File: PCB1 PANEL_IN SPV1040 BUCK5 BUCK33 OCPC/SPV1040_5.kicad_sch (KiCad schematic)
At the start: 14 parts, among them J6 SOLAR, U6 SPV1040TTR

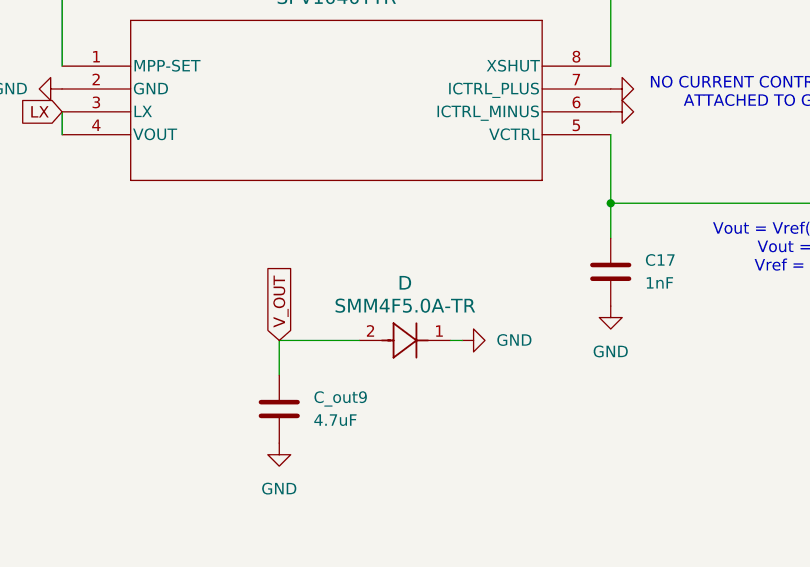
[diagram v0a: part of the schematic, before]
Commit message: Added some comments in POWERPCB, about bus interface
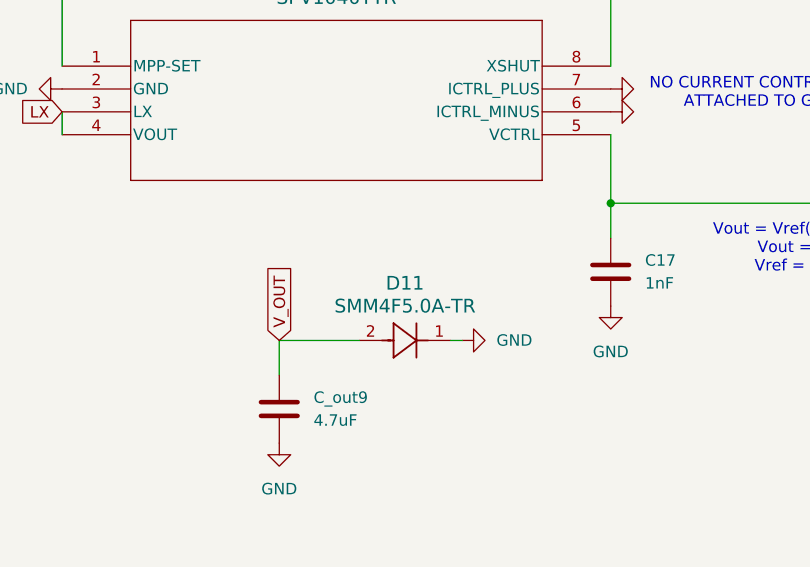
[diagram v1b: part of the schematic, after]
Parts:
- renumbered D to D11
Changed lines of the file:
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@@
 	(label "BAT_MON+"
 		(at 228.6 77.47 0)
-		(fields_autoplaced yes)
 		(effects
 			(font
@@
 		(dnp no)
 		(fields_autoplaced yes)
-		(property "Reference" "D"
+		(property "Reference" "D11"
 			(at 96.52 97.79 0)
 			(effects
@@
 		)
 		(instances
+			(project "PCB1 PANEL_IN SPV1040 BUCK5 BUCK33 OCPC"
+				(path "/494c9d9f-6b33-4248-a813-27ffaaa929bd/8c378675-f65a-4b67-963a-3f9cd3fefa7d"
+					(reference "D11")
+					(unit 1)
+				)
+			)
 			(project ""
 				(path "/e98ca604-2429-4c57-b4a1-3d03a5ec156e"
